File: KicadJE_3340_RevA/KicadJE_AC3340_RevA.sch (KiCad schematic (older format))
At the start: 127 parts, among them J101 RampOut1, J102 PulseOut2, J103 SawOut3, J104 In1.1, J105 In1.2, J106 In1.3, J107 SS_In2, J108 HS_In3, J109 FM_In4, J110 PWM_In5, J111 SineOut4, P101 HEADER_2x5_Doepfer, Q101 MMBT3906, Q102 UMX1N, SW101 Octave (3 state), U101 TL072, U102 TL072, U103 TL072, U104 AS3340, U105 L78L05_SOT89, U106 L79L05_SOT89, U107 TL072

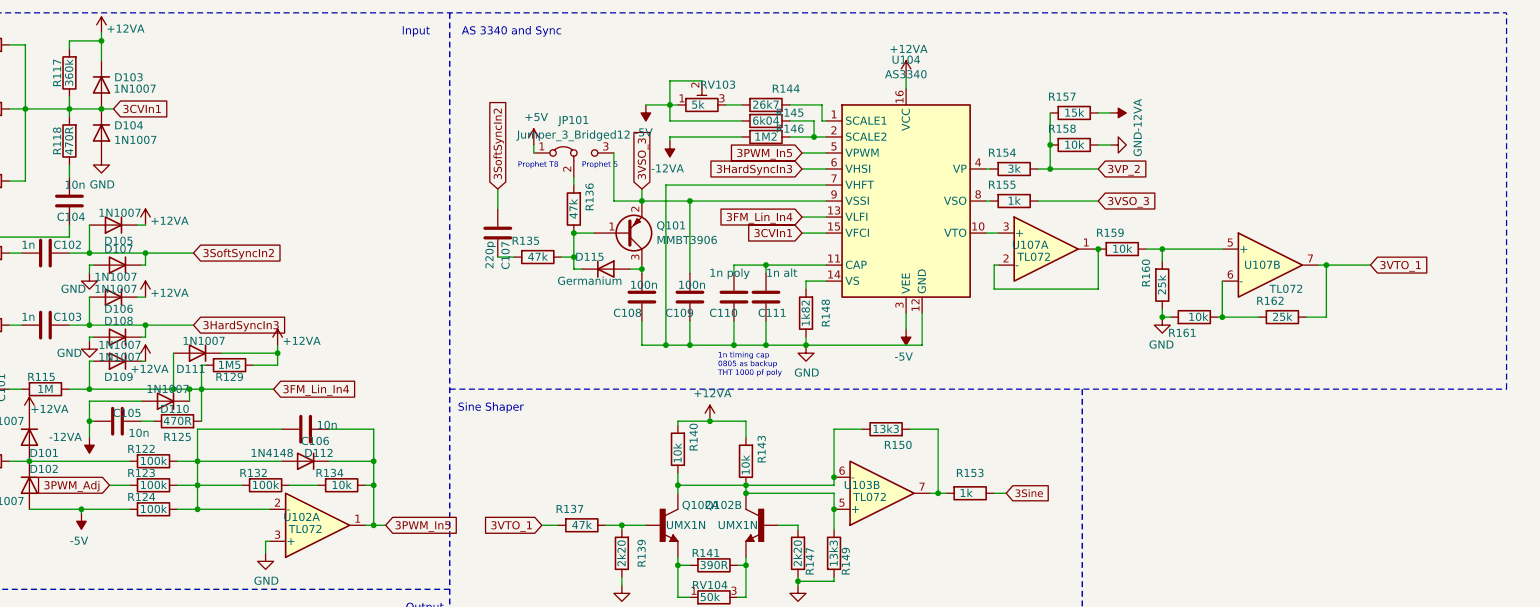
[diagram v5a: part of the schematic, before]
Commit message: Mounting holes in schematic
Prepare for next faceplate
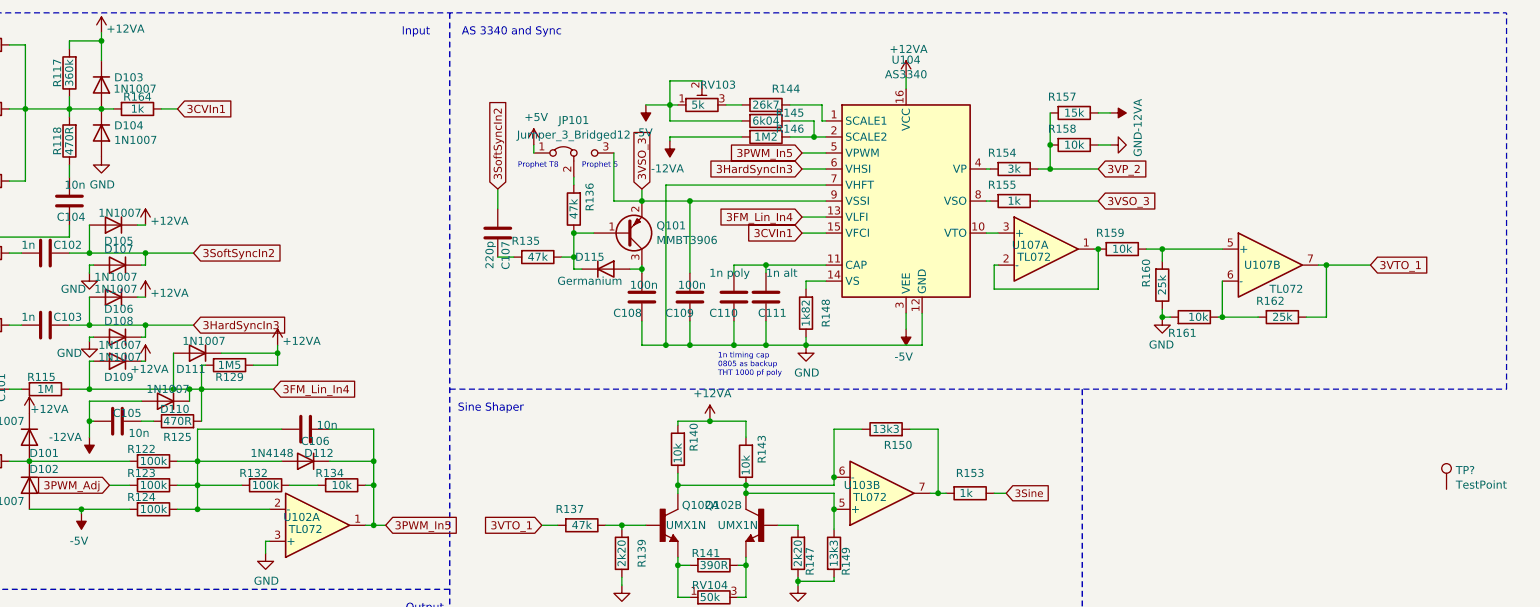
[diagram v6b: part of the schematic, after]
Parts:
- added R164: 1k, Resistor_SMD:R_0805_2012Metric_Pad1.15x1.40mm_HandSolder, symbol Device:R
- added TP?: TestPoint, symbol Connector:TestPoint
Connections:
- net 3CVIn1: now also R164.1; no longer D103.2 (A), D104.1 (K), R108.1, R109.1, R110.1, R117.1, R118.2
- new net: D103.2 (A), D104.1 (K), R108.1, R109.1, R110.1, R117.1, R118.2, R164.2
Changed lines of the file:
@@
 Wire Wire Line
 	1350 1225 1350 1025
-Text GLabel 2400 1125 2    50   Input ~ 0
+Text GLabel 2800 1125 2    50   Input ~ 0
 3CVIn1
 Wire Wire Line
@@
 Wire Wire Line
 	6750 5275 6875 5275
+$Comp
+L Device:R R164
+U 1 1 5EE442D5
+P 2550 1125
+AR Path="/5EE442D5" Ref="R164"  Part="1"
+AR Path="/5C8C5FC0/5EE442D5" Ref="R?"  Part="1"
+AR Path="/5CAAE8D3/5EE442D5" Ref="R?"  Part="1"
+AR Path="/5E4B0DD9/5EE442D5" Ref="R?"  Part="1"
+AR Path="/5F49A670/5EE442D5" Ref="R?"  Part="1"
+F 0 "R164" V 2475 1125 50  0000 C CNN
+F 1 "1k" V 2550 1125 50  0000 C CNN
+F 2 "Resistor_SMD:R_0805_2012Metric_Pad1.15x1.40mm_HandSolder" V 2480 1125 50  0001 C CNN
+F 3 "~" H 2550 1125 50  0001 C CNN
+	1    2550 1125
+	0    1    1    0
+$EndComp
+Wire Wire Line
+	2700 1125 2800 1125
+$Comp
+L Connector:TestPoint TP?
+U 1 1 5EE75A89
+P 10725 3500
+F 0 "TP?" H 10783 3618 50  0000 L CNN
+F 1 "TestPoint" H 10783 3527 50  0000 L CNN
+F 2 "" H 10925 3500 50  0001 C CNN
+F 3 "~" H 10925 3500 50  0001 C CNN
+	1    10725 3500
+	1    0    0    -1
+$EndComp
 $EndSCHEMATC

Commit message: LED hole
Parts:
- added TP101: Oct, AJ:Pot_6m3, symbol Connector:TestPoint
- added TP102: In1, AJ:Jack_6m3, symbol Connector:TestPoint
- added TP103: In2, AJ:Jack_6m3, symbol Connector:TestPoint
- added TP104: In3, AJ:Jack_6m3, symbol Connector:TestPoint
- added TP105: SS, AJ:Jack_6m3, symbol Connector:TestPoint
- added TP106: HS, AJ:Jack_6m3, symbol Connector:TestPoint
- added TP107: FM, AJ:Jack_6m3, symbol Connector:TestPoint
- added TP108: PWM, AJ:Jack_6m3, symbol Connector:TestPoint
- added TP110: SQ, AJ:Jack_6m3, symbol Connector:TestPoint
- added TP111: Saw, AJ:Jack_6m3, symbol Connector:TestPoint
- added TP112: Fine, AJ:Pot_6m3_scale1, symbol Connector:TestPoint
- added TP113: PWM, AJ:Pot_6m3_scale1, symbol Connector:TestPoint
- added TP114: ON, AJ:LED_Hole_2.5mm, symbol Connector:TestPoint
- added TP115: 3m5 jack, AJ:Jack_6m3, symbol Connector:TestPoint
- TP109: renamed from TP?; value TestPoint -> Tri; footprint (none) -> AJ:Jack_6m3
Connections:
- net GND: now also TP109.1, TP101.1, TP102.1, TP103.1, TP104.1, TP105.1, TP106.1, TP107.1, TP108.1, TP110.1, TP111.1, TP115.1
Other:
- moved on the sheet: TP109
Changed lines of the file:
@@
 $EndComp
 Wire Wire Line
-	1350 1025 1200 1025
+	1350 1025 1250 1025
 Wire Wire Line
 	1350 1025 1350 825
 Wire Wire Line
-	1350 625  1200 625
+	1350 625  1250 625
 Connection ~ 1350 1025
 Wire Wire Line
@@
 $EndComp
 Wire Wire Line
-	1325 5125 1175 5125
+	1325 5125 1250 5125
 Wire Wire Line
-	1325 4425 1175 4425
+	1325 4425 1250 4425
 Connection ~ 1325 5125
 Text GLabel 2900 2025 2    50   Input ~ 0
@@
 	1350 1225 1350 1475
 Wire Wire Line
-	1200 1475 1350 1475
+	1200 1475 1250 1475
 Wire Wire Line
 	1750 1575 1850 1575
@@
 	1350 1675 1350 1925
 Wire Wire Line
-	1200 1925 1350 1925
+	1200 1925 1250 1925
 Connection ~ 1350 1925
 Wire Wire Line
@@
 	1175 6025 1425 6025
 Wire Wire Line
-	1325 5925 1175 5925
+	1325 5925 1250 5925
 $Comp
 L Device:R R107
@@
 $EndComp
 Wire Wire Line
-	1350 2775 1200 2775
+	1350 2775 1250 2775
 Wire Wire Line
 	1350 2775 1350 2575
 Wire Wire Line
-	1350 2375 1200 2375
+	1350 2375 1250 2375
 Connection ~ 1350 2775
 Wire Wire Line
@@
 	1350 2975 1350 3225
 Wire Wire Line
-	1200 3225 1350 3225
+	1200 3225 1250 3225
 $Comp
 L Device:R R115
@@
 	2700 1125 2800 1125
 $Comp
-L Connector:TestPoint TP?
+L Connector:TestPoint TP109
 U 1 1 5EE75A89
-P 10725 3500
-F 0 "TP?" H 10783 3618 50  0000 L CNN
-F 1 "TestPoint" H 10783 3527 50  0000 L CNN
-F 2 "" H 10925 3500 50  0001 C CNN
-F 3 "~" H 10925 3500 50  0001 C CNN
-	1    10725 3500
+P 1250 4425
+F 0 "TP109" H 1308 4543 50  0000 L CNN
+F 1 "Tri" H 1308 4452 50  0000 L CNN
+F 2 "AJ:Jack_6m3" H 1450 4425 50  0001 C CNN
+F 3 "~" H 1450 4425 50  0001 C CNN
+	1    1250 4425
+	1    0    0    -1
+$EndComp
+$Comp
+L Connector:TestPoint TP115
+U 1 1 5EE78A77
+P 7625 4350
+F 0 "TP115" H 7683 4468 50  0000 L CNN
+F 1 "3m5 jack" H 7683 4377 50  0000 L CNN
+F 2 "AJ:Jack_6m3" H 7825 4350 50  0001 C CNN
+F 3 "~" H 7825 4350 50  0001 C CNN
+	1    7625 4350
+	1    0    0    -1
+$EndComp
+Connection ~ 7625 4350
+Connection ~ 1325 4425
+Connection ~ 1250 4425
+Wire Wire Line
+	1250 4425 1175 4425
+$Comp
+L Connector:TestPoint TP110
+U 1 1 5EEA7CE8
+P 1250 5125
+F 0 "TP110" H 1308 5243 50  0000 L CNN
+F 1 "SQ" H 1308 5152 50  0000 L CNN
+F 2 "AJ:Jack_6m3" H 1450 5125 50  0001 C CNN
+F 3 "~" H 1450 5125 50  0001 C CNN
+	1    1250 5125
+	1    0    0    -1
+$EndComp
+Connection ~ 1250 5125
+Wire Wire Line
+	1250 5125 1175 5125
+$Comp
+L Connector:TestPoint TP111
+U 1 1 5EEA8234
+P 1250 5925
+F 0 "TP111" H 1308 6043 50  0000 L CNN
+F 1 "Saw" H 1308 5952 50  0000 L CNN
+F 2 "AJ:Jack_6m3" H 1450 5925 50  0001 C CNN
+F 3 "~" H 1450 5925 50  0001 C CNN
+	1    1250 5925
+	1    0    0    -1
+$EndComp
+Connection ~ 1250 5925
+Wire Wire Line
+	1250 5925 1175 5925
+$Comp
+L Connector:TestPoint TP108
+U 1 1 5EEA874B
+P 1250 3225
+F 0 "TP108" H 1308 3343 50  0000 L CNN
+F 1 "PWM" H 1308 3252 50  0000 L CNN
+F 2 "AJ:Jack_6m3" H 1450 3225 50  0001 C CNN
+F 3 "~" H 1450 3225 50  0001 C CNN
+	1    1250 3225
+	1    0    0    -1
+$EndComp
+Connection ~ 1250 3225
+Wire Wire Line
+	1250 3225 1350 3225
+$Comp
+L Connector:TestPoint TP107
+U 1 1 5EEA8C5E
+P 1250 2775
+F 0 "TP107" H 1308 2893 50  0000 L CNN
+F 1 "FM" H 1308 2802 50  0000 L CNN
+F 2 "AJ:Jack_6m3" H 1450 2775 50  0001 C CNN
+F 3 "~" H 1450 2775 50  0001 C CNN
+	1    1250 2775
+	1    0    0    -1
+$EndComp
+Connection ~ 1250 2775
+Wire Wire Line
+	1250 2775 1200 2775
+$Comp
+L Connector:TestPoint TP106
+U 1 1 5EEA8E6B
+P 1250 2375
+F 0 "TP106" H 1308 2493 50  0000 L CNN
+F 1 "HS" H 1308 2402 50  0000 L CNN
+F 2 "AJ:Jack_6m3" H 1450 2375 50  0001 C CNN
+F 3 "~" H 1450 2375 50  0001 C CNN
+	1    1250 2375
+	1    0    0    -1
+$EndComp
+Connection ~ 1250 2375
+Wire Wire Line
+	1250 2375 1200 2375
+$Comp
+L Connector:TestPoint TP105
+U 1 1 5EEA9123
+P 1250 1925
+F 0 "TP105" H 1308 2043 50  0000 L CNN
+F 1 "SS" H 1308 1952 50  0000 L CNN
+F 2 "AJ:Jack_6m3" H 1450 1925 50  0001 C CNN
+F 3 "~" H 1450 1925 50  0001 C CNN
+	1    1250 1925
+	1    0    0    -1
+$EndComp
+Connection ~ 1250 1925
+Wire Wire Line
+	1250 1925 1350 1925
+$Comp
+L Connector:TestPoint TP104
+U 1 1 5EEA942D
+P 1250 1475
+F 0 "TP104" H 1308 1593 50  0000 L CNN
+F 1 "In3" H 1308 1502 50  0000 L CNN
+F 2 "AJ:Jack_6m3" H 1450 1475 50  0001 C CNN
+F 3 "~" H 1450 1475 50  0001 C CNN
+	1    1250 1475
+	1    0    0    -1
+$EndComp
+Connection ~ 1250 1475
+Wire Wire Line
+	1250 1475 1350 1475
+$Comp
+L Connector:TestPoint TP103
+U 1 1 5EEA9D54
+P 1250 1025
+F 0 "TP103" H 1308 1143 50  0000 L CNN
+F 1 "In2" H 1308 1052 50  0000 L CNN
+F 2 "AJ:Jack_6m3" H 1450 1025 50  0001 C CNN
+F 3 "~" H 1450 1025 50  0001 C CNN
+	1    1250 1025
+	1    0    0    -1
+$EndComp
+Connection ~ 1250 1025
+Wire Wire Line
+	1250 1025 1200 1025
+$Comp
+L Connector:TestPoint TP102
+U 1 1 5EEAA042
+P 1250 625
+F 0 "TP102" H 1308 743 50  0000 L CNN
+F 1 "In1" H 1308 652 50  0000 L CNN
+F 2 "AJ:Jack_6m3" H 1450 625 50  0001 C CNN
+F 3 "~" H 1450 625 50  0001 C CNN
+	1    1250 625
+	1    0    0    -1
+$EndComp
+Connection ~ 1250 625
+Wire Wire Line
+	1250 625  1200 625
+$Comp
+L Connector:TestPoint TP101
+U 1 1 5EEAA7A8
+P 850 7225
+F 0 "TP101" V 775 7325 50  0000 C CNN
+F 1 "Oct" V 725 7325 50  0000 C CNN
+F 2 "AJ:Pot_6m3" H 1050 7225 50  0001 C CNN
+F 3 "~" H 1050 7225 50  0001 C CNN
+	1    850  7225
+	0    -1   -1   0
+$EndComp
+Connection ~ 850  7225
+$Comp
+L Connector:TestPoint TP112
+U 1 1 5EEAB808
+P 2250 7375
+F 0 "TP112" H 2308 7493 50  0000 L CNN
+F 1 "Fine" H 2308 7402 50  0000 L CNN
+F 2 "AJ:Pot_6m3_scale1" H 2450 7375 50  0001 C CNN
+F 3 "~" H 2450 7375 50  0001 C CNN
+	1    2250 7375
+	1    0    0    -1
+$EndComp
+$Comp
+L Connector:TestPoint TP113
+U 1 1 5EEAC9DC
+P 4275 7175
+F 0 "TP113" H 4333 7293 50  0000 L CNN
+F 1 "PWM" H 4333 7202 50  0000 L CNN
+F 2 "AJ:Pot_6m3_scale1" H 4475 7175 50  0001 C CNN
+F 3 "~" H 4475 7175 50  0001 C CNN
+	1    4275 7175
+	1    0    0    -1
+$EndComp
+$Comp
+L Connector:TestPoint TP114
+U 1 1 5EEADEBD
+P 5600 6250
+F 0 "TP114" H 5658 6368 50  0000 L CNN
+F 1 "ON" H 5658 6277 50  0000 L CNN
+F 2 "AJ:LED_Hole_2.5mm" H 5800 6250 50  0001 C CNN
+F 3 "~" H 5800 6250 50  0001 C CNN
+	1    5600 6250
 	1    0    0    -1
 $EndComp

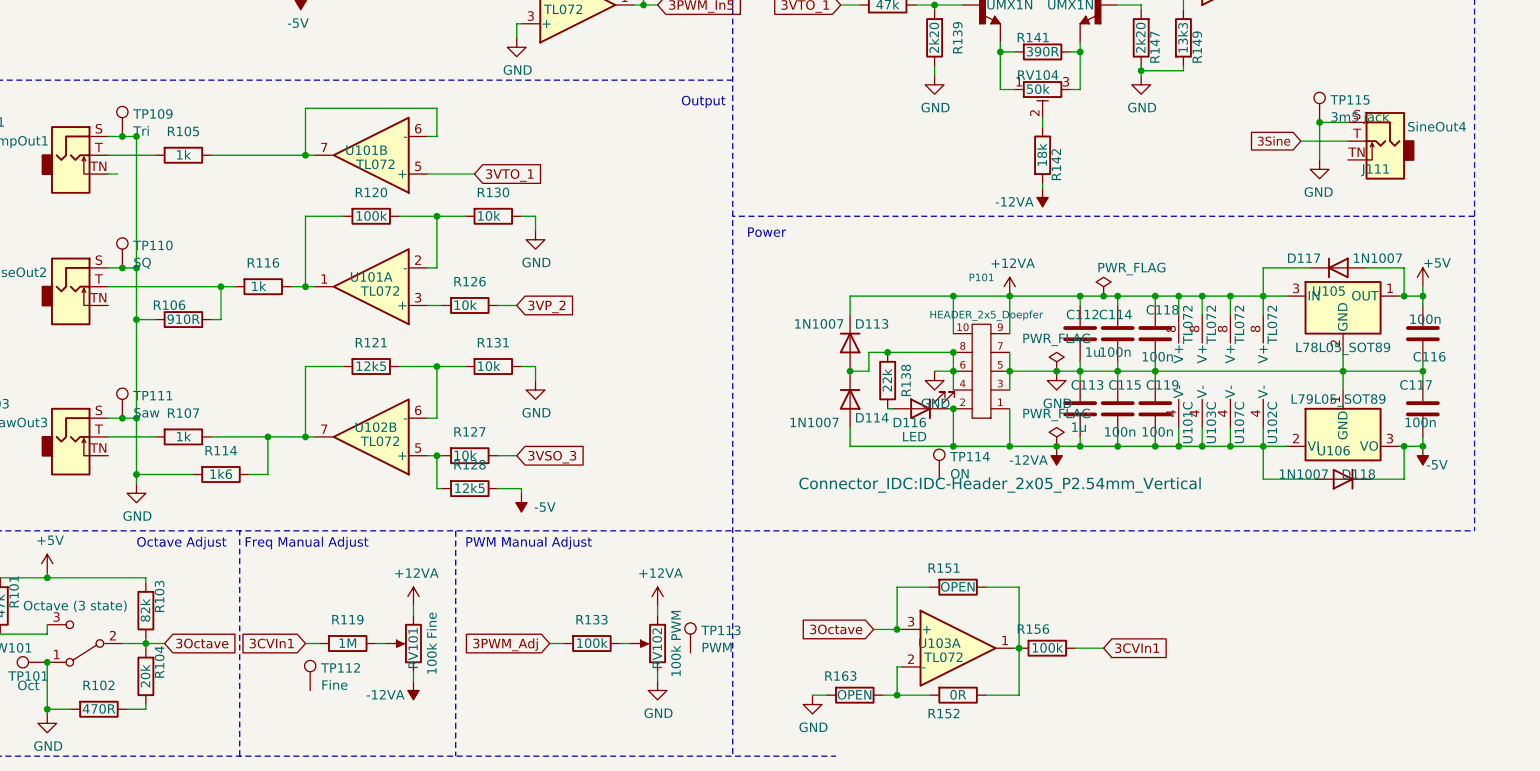
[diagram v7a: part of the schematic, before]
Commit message: TP -> mounting holes + ERC
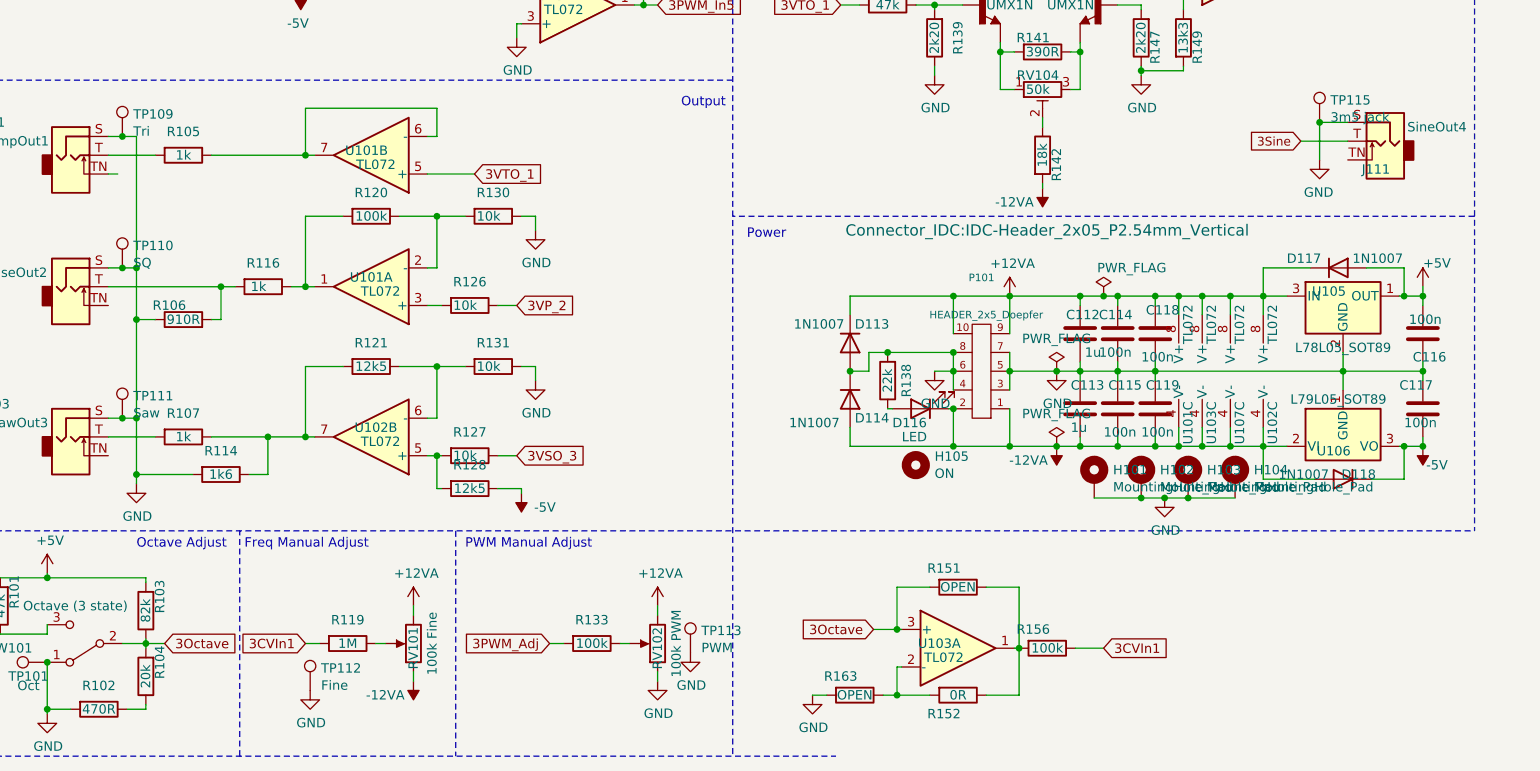
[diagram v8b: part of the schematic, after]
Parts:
- removed TP114: ON, AJ:LED_Hole_2.5mm, symbol Connector:TestPoint
- added H101, H102, H103, H104: MountingHole_Pad, AJ:MountingHole_Eurorack3, symbol Mechanical:MountingHole_Pad
- added H105: ON, AJ:LED_Hole_3mm, symbol Mechanical:MountingHole
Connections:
- net GND: now also TP112.1, TP113.1, H101.1, H102.1, H103.1, H104.1
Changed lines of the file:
@@
 F 0 "P101" H 5825 5177 40  0000 C CNN
 F 1 "HEADER_2x5_Doepfer" H 5800 5375 40  0000 C CNN
-F 2 "Connector_IDC:IDC-Header_2x05_P2.54mm_Vertical" H 5725 6275 60  0000 C CNN
+F 2 "Connector_IDC:IDC-Header_2x05_P2.54mm_Vertical" H 5475 4925 60  0000 C CNN
 F 3 "" H 5825 5675 60  0000 C CNN
 	1    5825 5675
@@
 $EndComp
 Connection ~ 7625 4350
-Connection ~ 1325 4425
 Connection ~ 1250 4425
 Wire Wire Line
@@
 $EndComp
 $Comp
-L Connector:TestPoint TP114
-U 1 1 5EEADEBD
-P 5600 6250
-F 0 "TP114" H 5658 6368 50  0000 L CNN
-F 1 "ON" H 5658 6277 50  0000 L CNN
-F 2 "AJ:LED_Hole_2.5mm" H 5800 6250 50  0001 C CNN
-F 3 "~" H 5800 6250 50  0001 C CNN
-	1    5600 6250
+L Mechanical:MountingHole_Pad H101
+U 1 1 5EF22F1C
+P 6425 6250
+F 0 "H101" H 6525 6299 50  0000 L CNN
+F 1 "MountingHole_Pad" H 6525 6208 50  0000 L CNN
+F 2 "AJ:MountingHole_Eurorack3" H 6425 6250 50  0001 C CNN
+F 3 "~" H 6425 6250 50  0001 C CNN
+	1    6425 6250
+	1    0    0    -1
+$EndComp
+$Comp
+L Mechanical:MountingHole_Pad H102
+U 1 1 5EF24A8F
+P 6675 6250
+F 0 "H102" H 6775 6299 50  0000 L CNN
+F 1 "MountingHole_Pad" H 6775 6208 50  0000 L CNN
+F 2 "AJ:MountingHole_Eurorack3" H 6675 6250 50  0001 C CNN
+F 3 "~" H 6675 6250 50  0001 C CNN
+	1    6675 6250
+	1    0    0    -1
+$EndComp
+$Comp
+L Mechanical:MountingHole_Pad H103
+U 1 1 5EF24C31
+P 6925 6250
+F 0 "H103" H 7025 6299 50  0000 L CNN
+F 1 "MountingHole_Pad" H 7025 6208 50  0000 L CNN
+F 2 "AJ:MountingHole_Eurorack3" H 6925 6250 50  0001 C CNN
+F 3 "~" H 6925 6250 50  0001 C CNN
+	1    6925 6250
+	1    0    0    -1
+$EndComp
+$Comp
+L Mechanical:MountingHole_Pad H104
+U 1 1 5EF24E1C
+P 7175 6250
+F 0 "H104" H 7275 6299 50  0000 L CNN
+F 1 "MountingHole_Pad" H 7275 6208 50  0000 L CNN
+F 2 "AJ:MountingHole_Eurorack3" H 7175 6250 50  0001 C CNN
+F 3 "~" H 7175 6250 50  0001 C CNN
+	1    7175 6250
+	1    0    0    -1
+$EndComp
+Wire Wire Line
+	7175 6350 6925 6350
+Connection ~ 6675 6350
+Wire Wire Line
+	6675 6350 6425 6350
+Connection ~ 6925 6350
+$Comp
+L Envelope-cache-2018-08-04-13-00-04:GND #PWR0120
+U 1 1 5EF57B05
+P 6800 6350
+AR Path="/5EF57B05" Ref="#PWR0120"  Part="1"
+AR Path="/5C8C5FC0/5EF57B05" Ref="#PWR?"  Part="1"
+AR Path="/5CAAE8D3/5EF57B05" Ref="#PWR?"  Part="1"
+AR Path="/5E4B0DD9/5EF57B05" Ref="#PWR?"  Part="1"
+AR Path="/5E62ACA1/5EF57B05" Ref="#PWR?"  Part="1"
+AR Path="/5F49A670/5EF57B05" Ref="#PWR?"  Part="1"
+F 0 "#PWR0120" H 6800 6100 50  0001 C CNN
+F 1 "GND" H 6805 6177 50  0000 C CNN
+F 2 "" H 6800 6350 50  0001 C CNN
+F 3 "" H 6800 6350 50  0001 C CNN
+	1    6800 6350
+	1    0    0    -1
+$EndComp
+Connection ~ 6800 6350
+Wire Wire Line
+	6800 6350 6675 6350
+Wire Wire Line
+	6800 6350 6925 6350
+$Comp
+L Envelope-cache-2018-08-04-13-00-04:GND #PWR0147
+U 1 1 5EF95D3D
+P 4275 7175
+AR Path="/5EF95D3D" Ref="#PWR0147"  Part="1"
+AR Path="/5C8C5FC0/5EF95D3D" Ref="#PWR?"  Part="1"
+AR Path="/5CAAE8D3/5EF95D3D" Ref="#PWR?"  Part="1"
+AR Path="/5E4B0DD9/5EF95D3D" Ref="#PWR?"  Part="1"
+AR Path="/5E62ACA1/5EF95D3D" Ref="#PWR?"  Part="1"
+AR Path="/5F49A670/5EF95D3D" Ref="#PWR?"  Part="1"
+F 0 "#PWR0147" H 4275 6925 50  0001 C CNN
+F 1 "GND" H 4280 7002 50  0000 C CNN
+F 2 "" H 4275 7175 50  0001 C CNN
+F 3 "" H 4275 7175 50  0001 C CNN
+	1    4275 7175
+	1    0    0    -1
+$EndComp
+$Comp
+L Envelope-cache-2018-08-04-13-00-04:GND #PWR0146
+U 1 1 5EF966DD
+P 2250 7375
+AR Path="/5EF966DD" Ref="#PWR0146"  Part="1"
+AR Path="/5C8C5FC0/5EF966DD" Ref="#PWR?"  Part="1"
+AR Path="/5CAAE8D3/5EF966DD" Ref="#PWR?"  Part="1"
+AR Path="/5E4B0DD9/5EF966DD" Ref="#PWR?"  Part="1"
+AR Path="/5E62ACA1/5EF966DD" Ref="#PWR?"  Part="1"
+AR Path="/5F49A670/5EF966DD" Ref="#PWR?"  Part="1"
+F 0 "#PWR0146" H 2250 7125 50  0001 C CNN
+F 1 "GND" H 2255 7202 50  0000 C CNN
+F 2 "" H 2250 7375 50  0001 C CNN
+F 3 "" H 2250 7375 50  0001 C CNN
+	1    2250 7375
+	1    0    0    -1
+$EndComp
+$Comp
+L Mechanical:MountingHole H105
+U 1 1 5EF9702E
+P 5475 6175
+F 0 "H105" H 5575 6221 50  0000 L CNN
+F 1 "ON" H 5575 6130 50  0000 L CNN
+F 2 "AJ:LED_Hole_3mm" H 5475 6175 50  0001 C CNN
+F 3 "~" H 5475 6175 50  0001 C CNN
+	1    5475 6175
 	1    0    0    -1
 $EndComp
